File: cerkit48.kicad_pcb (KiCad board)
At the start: 2 copper layers, 251.5 x 128.3 mm, 104 parts, among them J1 I2C, SW1 SW_Push_Dual_x2, SW10 CherryMX, SW11 CherryMX, SW12 CherryMX, SW13 CherryMX, SW14 CherryMX, SW15 CherryMX, SW16 CherryMX, SW17 CherryMX, SW18 CherryMX, SW19 CherryMX, SW2 CherryMX, SW20 CherryMX, SW21 CherryMX, SW22 CherryMX, SW23 CherryMX, SW24 CherryMX, SW25 CherryMX, SW26 CherryMX, SW27 CherryMX, SW28 CherryMX, SW29 CherryMX, SW3 CherryMX, SW30 CherryMX, SW31 CherryMX, SW32 CherryMX, SW33 CherryMX, SW34 CherryMX, SW35 CherryMX, SW36 CherryMX, SW37 CherryMX, SW38 CherryMX, SW39 CherryMX, SW4 CherryMX, SW40 CherryMX, SW41 CherryMX, SW42 CherryMX, SW43 CherryMX, SW44 CherryMX, SW45 CherryMX, SW46 CherryMX, SW47 CherryMX, SW48 CherryMX, SW49 CherryMX, SW5 CherryMX, SW6 CherryMX, SW7 CherryMX, SW8 CherryMX, SW9 CherryMX, U1 proton_c

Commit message: Updated schematic to use project symbols from submodules
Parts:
- J1: footprint footprints:PIN_HEADER_I2C -> cerkit48:PIN_HEADER_I2C
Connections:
- D10 pad 1: ROW0 -> Net-(D10-Pad1)
- D11 pad 1: ROW0 -> Net-(D11-Pad1)
- D12 pad 1: ROW0 -> Net-(D12-Pad1)
- D14 pad 1: ROW1 -> Net-(D14-Pad1)
- D15 pad 1: ROW1 -> Net-(D15-Pad1)
- D16 pad 1: ROW1 -> Net-(D16-Pad1)
- D17 pad 1: ROW1 -> Net-(D17-Pad1)
- D18 pad 1: ROW1 -> Net-(D18-Pad1)
- D19 pad 1: ROW1 -> Net-(D19-Pad1)
- D2 pad 1: ROW0 -> Net-(D2-Pad1)
- D20 pad 1: ROW1 -> Net-(D20-Pad1)
- D21 pad 1: ROW1 -> Net-(D21-Pad1)
- D22 pad 1: ROW1 -> Net-(D22-Pad1)
- D23 pad 1: ROW1 -> Net-(D23-Pad1)
- D24 pad 1: ROW1 -> Net-(D24-Pad1)
- D26 pad 1: ROW2 -> Net-(D26-Pad1)
- D27 pad 1: ROW2 -> Net-(D27-Pad1)
- D28 pad 1: ROW2 -> Net-(D28-Pad1)
- D29 pad 1: ROW2 -> Net-(D29-Pad1)
- D3 pad 1: ROW0 -> Net-(D3-Pad1)
- D30 pad 1: ROW2 -> Net-(D30-Pad1)
- D31 pad 1: ROW2 -> Net-(D31-Pad1)
- D32 pad 1: ROW2 -> Net-(D32-Pad1)
- D33 pad 1: ROW2 -> Net-(D33-Pad1)
- D34 pad 1: ROW2 -> Net-(D34-Pad1)
- D35 pad 1: ROW2 -> Net-(D35-Pad1)
- D36 pad 1: ROW2 -> Net-(D36-Pad1)
- D38 pad 1: ROW3 -> Net-(D38-Pad1)
- D39 pad 1: ROW3 -> Net-(D39-Pad1)
- D4 pad 1: ROW0 -> Net-(D4-Pad1)
- D40 pad 1: ROW3 -> Net-(D40-Pad1)
- D41 pad 1: ROW3 -> Net-(D41-Pad1)
- D42 pad 1: ROW3 -> Net-(D42-Pad1)
- D43 pad 1: ROW3 -> Net-(D43-Pad1)
- D44 pad 1: ROW3 -> Net-(D44-Pad1)
- D45 pad 1: ROW3 -> Net-(D45-Pad1)
- D46 pad 1: ROW3 -> Net-(D46-Pad1)
- D47 pad 1: ROW3 -> Net-(D47-Pad1)
- D48 pad 1: ROW3 -> Net-(D48-Pad1)
- D5 pad 1: ROW0 -> Net-(D5-Pad1)
- D6 pad 1: ROW0 -> Net-(D6-Pad1)
- D7 pad 1: ROW0 -> Net-(D7-Pad1)
- D8 pad 1: ROW0 -> Net-(D8-Pad1)
- D9 pad 1: ROW0 -> Net-(D9-Pad1)

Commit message: reworked back traces
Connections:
- D10 pad 1: Net-(D10-Pad1) -> ROW0
- D11 pad 1: Net-(D11-Pad1) -> ROW0
- D12 pad 1: Net-(D12-Pad1) -> ROW0
- D14 pad 1: Net-(D14-Pad1) -> ROW1
- D15 pad 1: Net-(D15-Pad1) -> ROW1
- D16 pad 1: Net-(D16-Pad1) -> ROW1
- D17 pad 1: Net-(D17-Pad1) -> ROW1
- D18 pad 1: Net-(D18-Pad1) -> ROW1
- D19 pad 1: Net-(D19-Pad1) -> ROW1
- D2 pad 1: Net-(D2-Pad1) -> ROW0
- D20 pad 1: Net-(D20-Pad1) -> ROW1
- D21 pad 1: Net-(D21-Pad1) -> ROW1
- D22 pad 1: Net-(D22-Pad1) -> ROW1
- D23 pad 1: Net-(D23-Pad1) -> ROW1
- D24 pad 1: Net-(D24-Pad1) -> ROW1
- D26 pad 1: Net-(D26-Pad1) -> ROW2
- D27 pad 1: Net-(D27-Pad1) -> ROW2
- D28 pad 1: Net-(D28-Pad1) -> ROW2
- D29 pad 1: Net-(D29-Pad1) -> ROW2
- D3 pad 1: Net-(D3-Pad1) -> ROW0
- D30 pad 1: Net-(D30-Pad1) -> ROW2
- D31 pad 1: Net-(D31-Pad1) -> ROW2
- D32 pad 1: Net-(D32-Pad1) -> ROW2
- D33 pad 1: Net-(D33-Pad1) -> ROW2
- D34 pad 1: Net-(D34-Pad1) -> ROW2
- D35 pad 1: Net-(D35-Pad1) -> ROW2
- D36 pad 1: Net-(D36-Pad1) -> ROW2
- D38 pad 1: Net-(D38-Pad1) -> ROW3
- D39 pad 1: Net-(D39-Pad1) -> ROW3
- D4 pad 1: Net-(D4-Pad1) -> ROW0
- D40 pad 1: Net-(D40-Pad1) -> ROW3
- D41 pad 1: Net-(D41-Pad1) -> ROW3
- D42 pad 1: Net-(D42-Pad1) -> ROW3
- D43 pad 1: Net-(D43-Pad1) -> ROW3
- D44 pad 1: Net-(D44-Pad1) -> ROW3
- D45 pad 1: Net-(D45-Pad1) -> ROW3
- D46 pad 1: Net-(D46-Pad1) -> ROW3
- D47 pad 1: Net-(D47-Pad1) -> ROW3
- D48 pad 1: Net-(D48-Pad1) -> ROW3
- D5 pad 1: Net-(D5-Pad1) -> ROW0
- D6 pad 1: Net-(D6-Pad1) -> ROW0
- D7 pad 1: Net-(D7-Pad1) -> ROW0
- D8 pad 1: Net-(D8-Pad1) -> ROW0
- D9 pad 1: Net-(D9-Pad1) -> ROW0
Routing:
- net COL8: track 125.7 -> 115.2 mm
- net COL10: track 159.7 -> 149.8 mm
- net COL9: track 141.5 -> 131.8 mm
- net COL11: track 175.6 -> 165.9 mm
- net COL7: track 114.2 -> 107.6 mm
- net COL4: track 107.2 -> 104.3 mm
- net COL5: track 97.7 -> 96.0 mm
- net COL6: track 98.1 -> 99.4 mm

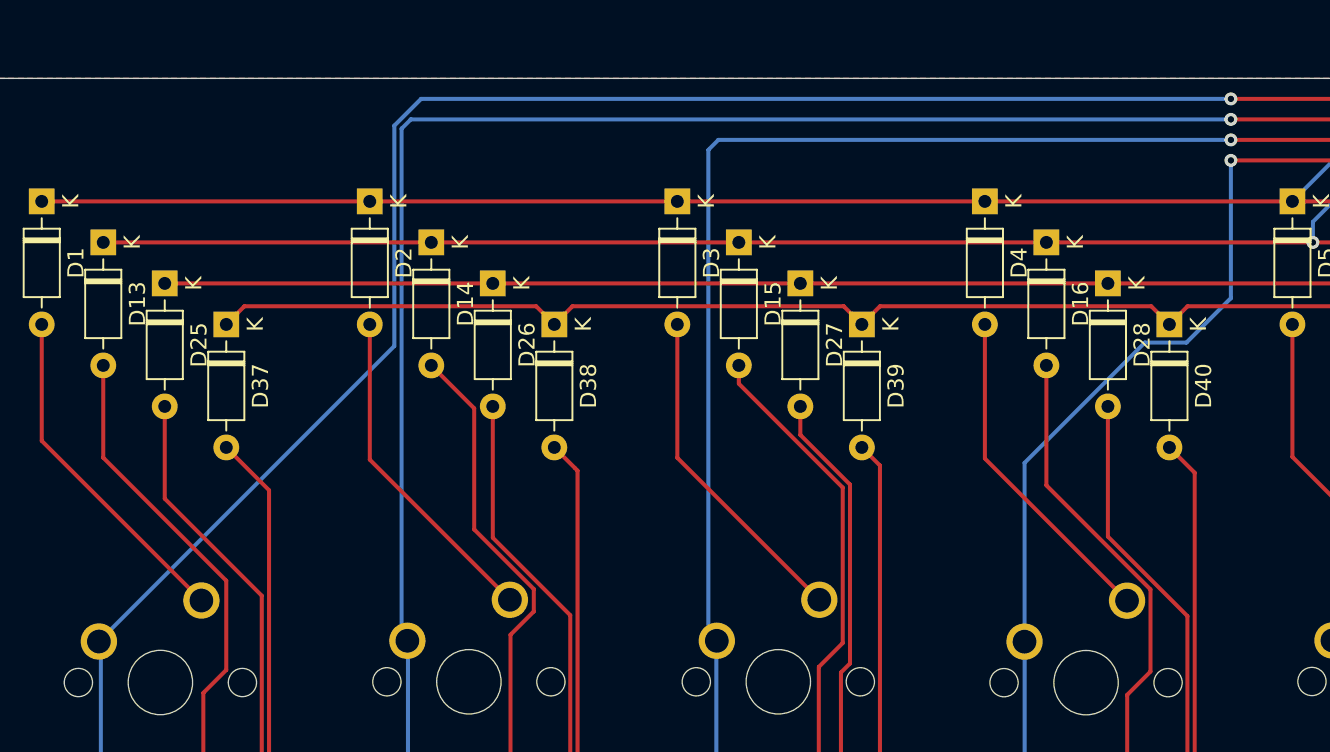
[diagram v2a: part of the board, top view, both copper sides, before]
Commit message: reworked back traces
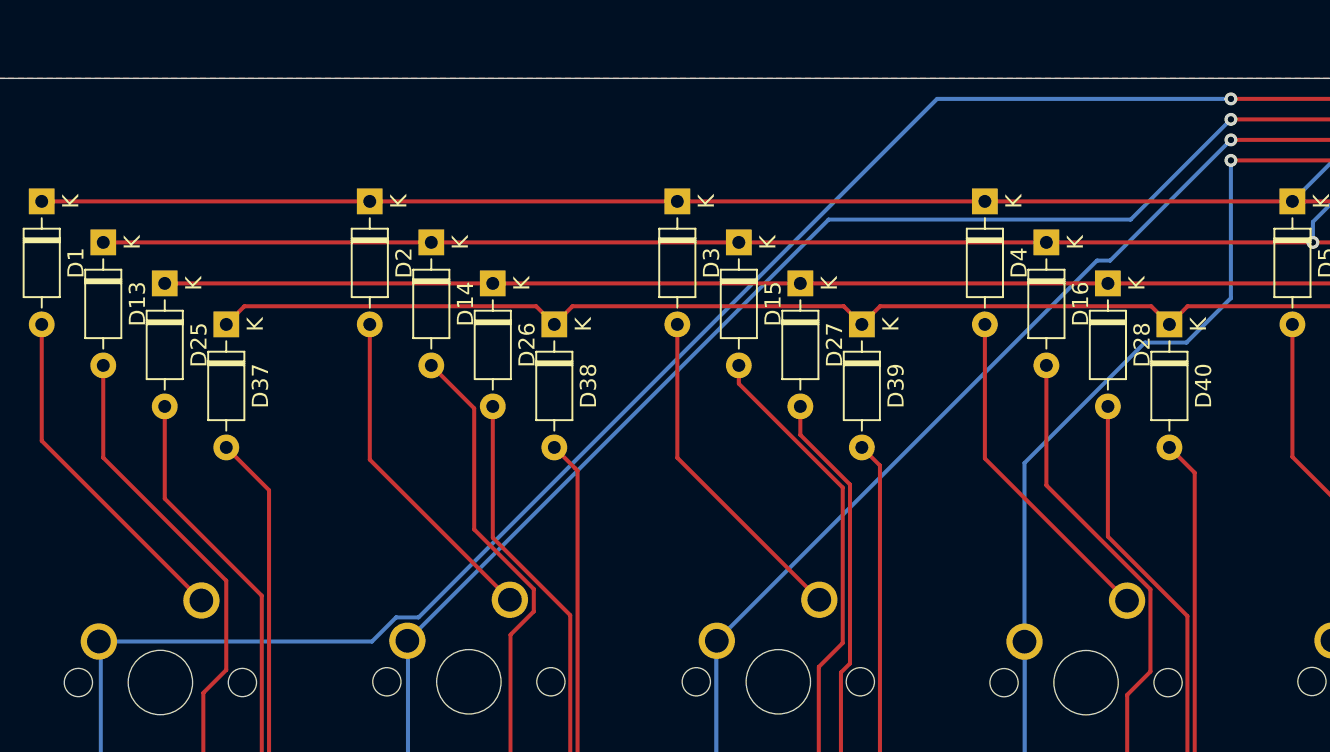
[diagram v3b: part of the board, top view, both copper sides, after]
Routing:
- net COL1: track 162.8 -> 143.1 mm
- net COL2: track 145.5 -> 126.4 mm
- net COL0: track 166.7 -> 158.7 mm
